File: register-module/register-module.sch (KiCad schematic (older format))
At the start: 0 parts

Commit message: Complete A register schematics
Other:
- note added: "Instruction Register"
- note added: "Register A"
- note added: "Register B"
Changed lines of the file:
@@
 EESchema Schematic File Version 4
+LIBS:register-module-cache
 EELAYER 29 0
 EELAYER END
 $Descr A4 11693 8268
 encoding utf-8
-Sheet 1 1
+Sheet 1 2
 Title "Register module"
 Date "2019-07-13"
@@
 Comment4 ""
 $EndDescr
+Wire Notes Line
+	475  4250 11200 4250
+Wire Notes Line
+	5350 475  5350 7775
+Text Notes 600  750  0    79   ~ 16
+Register A
+Text Notes 625  4550 0    79   ~ 16
+Register B
+Text Notes 5525 750  0    79   ~ 16
+Instruction Register
+$Sheet
+S 1525 1375 2175 1925
+U 5D2C3550
+F0 "a-register" 79
+F1 "a-register.sch" 79
+$EndSheet
 $EndSCHEMATC

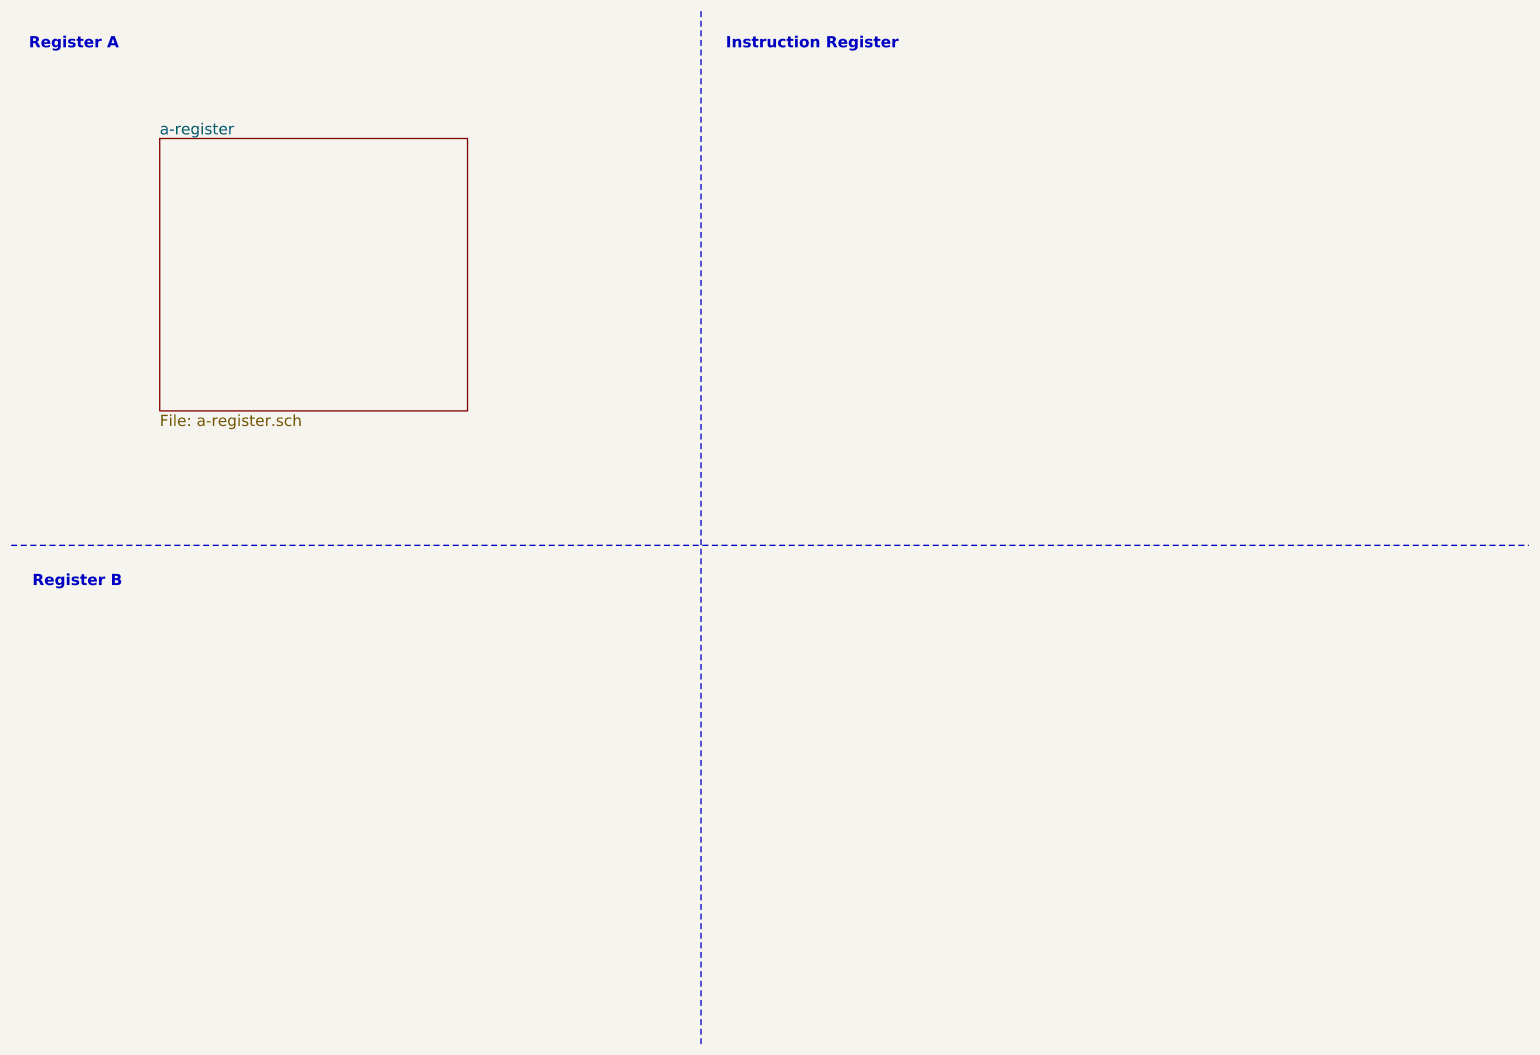
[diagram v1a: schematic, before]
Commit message: Register module complete, add project library folder
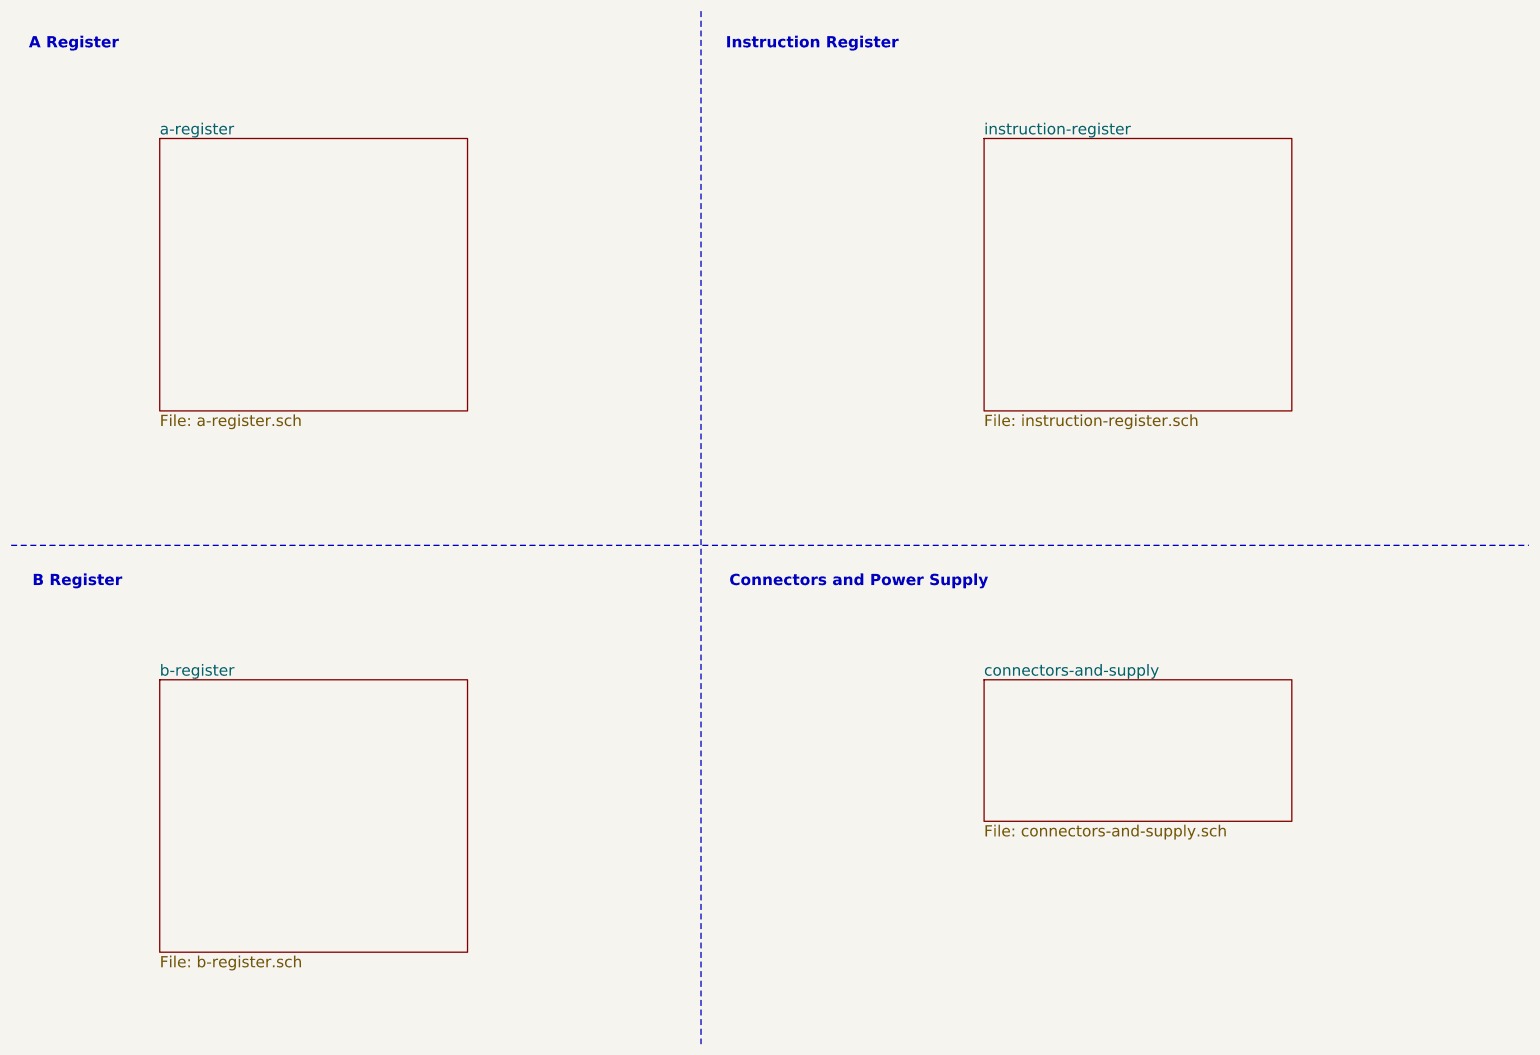
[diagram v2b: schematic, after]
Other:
- note added: "A Register"
- note added: "B Register"
- note added: "Connectors and Power Supply"
- note removed: "Register A"
- note removed: "Register B"
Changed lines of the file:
@@
 $Descr A4 11693 8268
 encoding utf-8
-Sheet 1 2
+Sheet 1 5
 Title "Register module"
 Date "2019-07-13"
@@
 $EndDescr
 Wire Notes Line
-	475  4250 11200 4250
-Wire Notes Line
 	5350 475  5350 7775
 Text Notes 600  750  0    79   ~ 16
-Register A
+A Register
 Text Notes 625  4550 0    79   ~ 16
-Register B
+B Register
 Text Notes 5525 750  0    79   ~ 16
 Instruction Register
@@
 F1 "a-register.sch" 79
 $EndSheet
+$Sheet
+S 1525 5200 2175 1925
+U 5D3D7580
+F0 "b-register" 79
+F1 "b-register.sch" 79
+$EndSheet
+Wire Notes Line
+	475  4250 11200 4250
+$Sheet
+S 7350 1375 2175 1925
+U 5D3F6C40
+F0 "instruction-register" 79
+F1 "instruction-register.sch" 79
+$EndSheet
+Text Notes 5550 4550 0    79   ~ 16
+Connectors and Power Supply
+$Sheet
+S 7350 5200 2175 1000
+U 5D5B01C2
+F0 "connectors-and-supply" 79
+F1 "connectors-and-supply.sch" 79
+$EndSheet
 $EndSCHEMATC
